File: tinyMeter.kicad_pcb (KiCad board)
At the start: 2 copper layers, 74.6 x 70 mm, 93 parts, among them J1 USB_MASTER, J2 DC_POWER, J3 USB_POWER, J4 USBA_OUT_2, J5 USBA_OUT_1, J6 DC_POWER, J7 Debug, J8 External antenna, Q1 100N03A, Q2 100N03A, Q3 100N03A, Q4 SS8050, SW1 SW_Push, SW2 SW_Push, SW3 SW_Push, SW4 SW_Push, SW5 SW_Push, SW6 Boot, SW7 Reset, U1 ESP32-S3, U2 INA219AxD, U3 INA219AxD, U4 INA219AxD, U5 AMS1117-3.3, Y1 Crystal_GND24

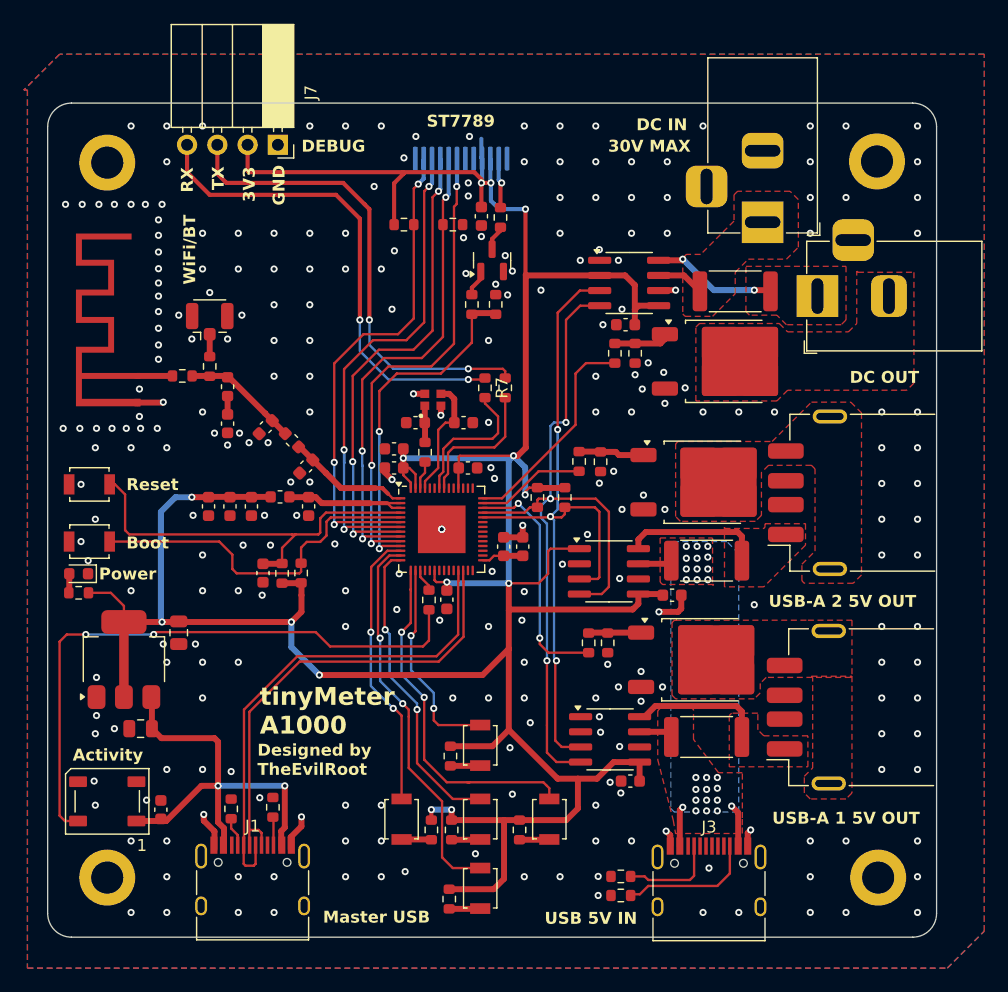
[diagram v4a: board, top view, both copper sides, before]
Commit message: Fix display connector orientation
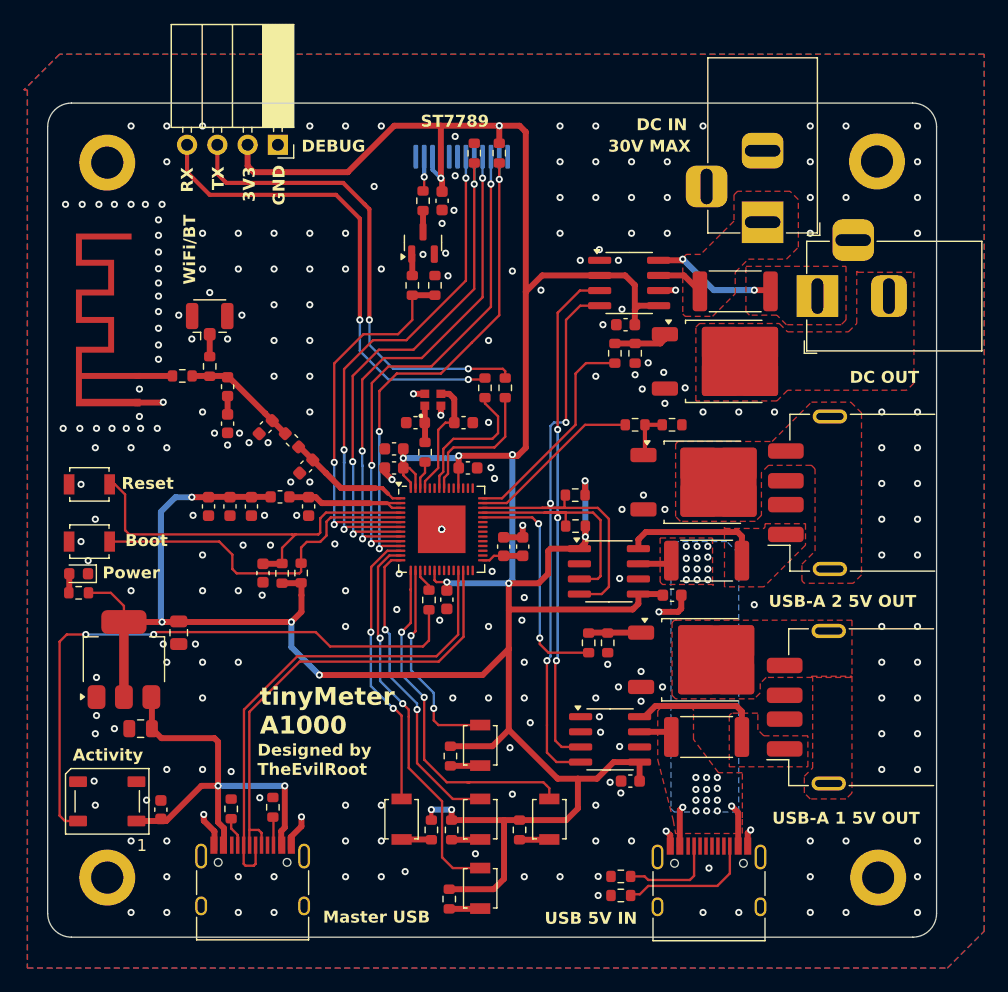
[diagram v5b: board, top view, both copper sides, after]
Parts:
- moved R34 10.0 mm to (176.9, 78.6), turned to -90 degrees
- moved DS1 8.84 mm to (173.8, 83.4), turned to 0 degrees
- moved R22 6.75 mm to (191.4, 101.4), turned to 0 degrees
- moved R30 6.65 mm to (170.5, 82.6)
- moved R33 6.26 mm to (174.8, 78.6), turned to 90 degrees
- moved Q4 5.98 mm to (170.5, 86.1)
- moved R21 5.62 mm to (188.3, 101.4), turned to 180 degrees
- moved R32 5.35 mm to (171.5, 89.7)
- moved R31 5.25 mm to (169.6, 89.7)
- moved R27 4.00 mm to (183.3, 109.9), turned to 0 degrees
- moved C6 3.55 mm to (172.1, 82.6)
- moved R26 0.90 mm to (183.3, 107.3), turned to 0 degrees
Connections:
- R26 pad 1: /METER_SDA -> /METER_SCL
- R27 pad 1: /METER_SCL -> /METER_SDA
- U1 pad 10: /DISPLAY_DC -> /DISPLAY_SDA
- U1 pad 11: /DISPLAY_BLK -> /DISPLAY_RST
- U1 pad 38: /METER_SDA -> /USBA_OUT_1_FETGATE
- U1 pad 39: /METER_SCL -> /METER_SDA
- U1 pad 40: /USBA_OUT_1_FETGATE -> /METER_SCL
- U1 pad 6: /DISPLAY_RST -> /DISPLAY_BLK
- U1 pad 7: /DISPLAY_SDA -> /DISPLAY_DC
- U1 pad 8: /DISPLAY_SCK -> /DISPLAY_CS
- U1 pad 9: /DISPLAY_CS -> /DISPLAY_SCK
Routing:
- net /USBA_OUT_2_FETGATE: track 9.19 -> 14.7 mm
- net /DISPLAY_CS: track 40.1 -> 43.4 mm
- net /DISPLAY_DC: track 39.9 -> 43.1 mm
- net /DISPLAY_BLK: track 29.1 -> 31.3 mm
- net /METER_SDA: track 61.0 -> 62.7 mm
- net /USBA_OUT2_GATE: track 5.52 -> 4.04 mm
- net /DISPLAY_LEDK: track 4.26 -> 2.92 mm
- net /DISPLAY_RST: track 41.2 -> 42.6 mm
- net /METER_SCL: track 65.5 -> 66.8 mm
- net /DISPLAY_SCK: track 40.3 -> 41.4 mm
- net /USBA_OUT_1_FETGATE: track 20.1 -> 19.3 mm
- net +3V3: track 278.8 -> 279.4 mm, vias 14 -> 15
- net GND: vias 240 -> 226

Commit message: Remove most of knockouts from silkscreen
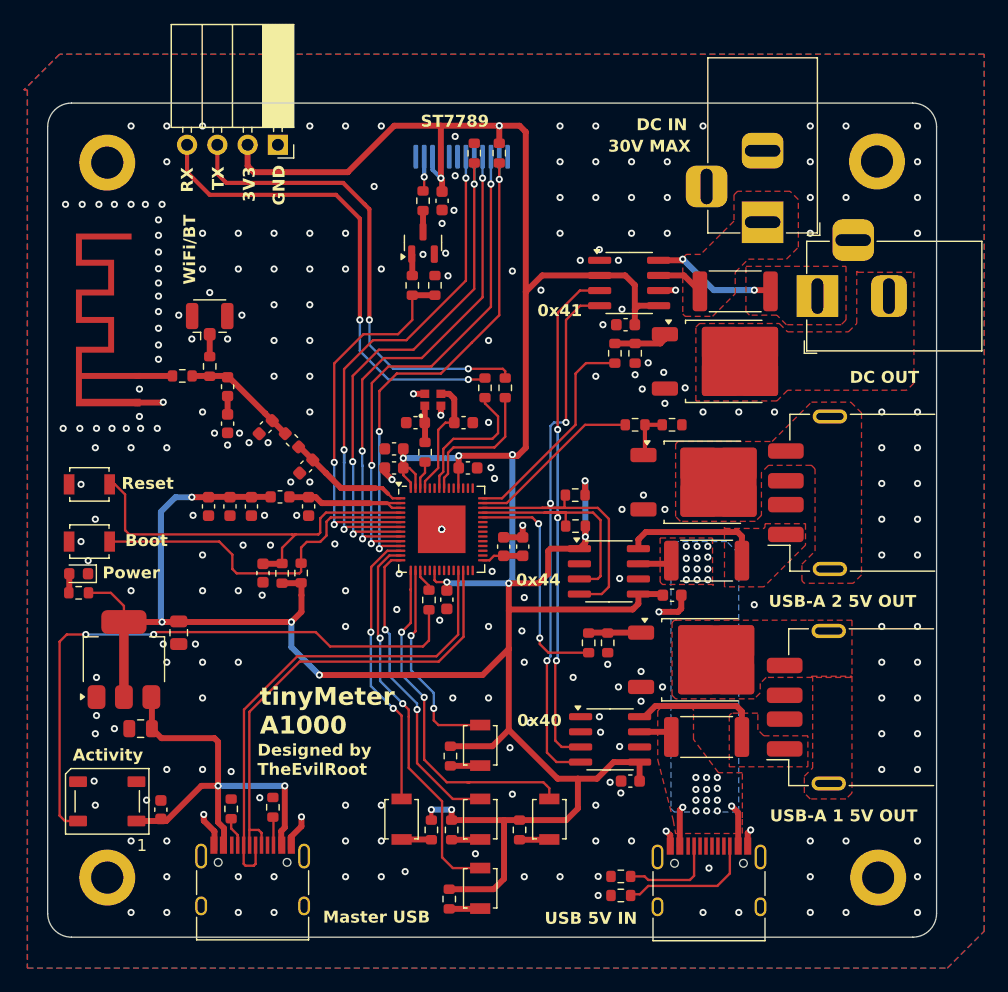
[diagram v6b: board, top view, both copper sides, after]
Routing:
- net GND: vias 226 -> 225
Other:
- board text added: "0x40"
- board text added: "0x41"
- board text added: "0x44"
- board text removed: "DEBUG"
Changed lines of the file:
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@@
 			(layer "F.SilkS"
 				(type "Top Silk Screen")
-				(color "White")
+				(color "Black")
 			)
 			(layer "F.Paste"
@@
 			(layer "F.Mask"
 				(type "Top Solder Mask")
-				(color "Black")
+				(color "White")
 				(thickness 0.01)
 			)
@@
 			(layer "B.Mask"
 				(type "Bottom Solder Mask")
-				(color "Black")
+				(color "White")
 				(thickness 0.01)
 			)
@@
 			(layer "B.SilkS"
 				(type "Bottom Silk Screen")
-				(color "White")
+				(color "Black")
 			)
 			(copper_finish "None")
@@
 		)
 	)
-	(gr_text "DEBUG"
-		(at 160.3 78.6 0)
-		(layer "F.SilkS" knockout)
-		(effects
-			(font
-				(size 1 1)
-				(thickness 0.2)
-				(bold yes)
-			)
-			(justify left bottom)
-		)
-	)
 	(gr_text "ST7789"
 		(at 170.3 76.5 0)
@@
 	)
 	(gr_text "USB-A 1 5V OUT"
-		(at 199.8 135 0)
-		(layer "F.SilkS" knockout)
+		(at 199.6 134.8 0)
+		(layer "F.SilkS")
 		(effects
 			(font
@@
 	(gr_text "Master USB"
 		(at 162.1 143.3 0)
-		(layer "F.SilkS" knockout)
+		(layer "F.SilkS")
 		(effects
 			(font
@@
 	(gr_text "3V3"
 		(at 156.5 82.7 90)
-		(layer "F.SilkS" knockout)
+		(layer "F.SilkS")
 		(effects
 			(font
@@
 	(gr_text "DC OUT"
 		(at 206.3 98 0)
-		(layer "F.SilkS" knockout)
+		(layer "F.SilkS")
 		(effects
 			(font
@@
 		)
 	)
+	(gr_text "0x41"
+		(at 180.1 92.4 0)
+		(layer "F.SilkS")
+		(effects
+			(font
+				(size 1 1)
+				(thickness 0.25)
+				(bold yes)
+			)
+			(justify left bottom)
+		)
+	)
 	(gr_text "GND"
 		(at 159 83 90)
-		(layer "F.SilkS" knockout)
+		(layer "F.SilkS")
 		(effects
 			(font
@@
 	(gr_text "Activity"
 		(at 141.1 129.7 0)
-		(layer "F.SilkS" knockout)
+		(layer "F.SilkS")
 		(effects
 			(font
@@
 	(gr_text "Reset"
 		(at 145.2 106.9 0)
-		(layer "F.SilkS" knockout)
+		(layer "F.SilkS")
 		(effects
 			(font
@@
 	(gr_text "DC IN"
 		(at 188.4 76.8 0)
-		(layer "F.SilkS" knockout)
+		(layer "F.SilkS")
 		(effects
 			(font
@@
 	(gr_text "Boot\n"
 		(at 145.5 111.7 0)
-		(layer "F.SilkS" knockout)
+		(layer "F.SilkS")
 		(effects
 			(font
@@
 	(gr_text "TX"
 		(at 153.9 81.7 90)
-		(layer "F.SilkS" knockout)
+		(layer "F.SilkS")
 		(effects
 			(font
@@
 		)
 	)
+	(gr_text "0x40"
+		(at 178.4 126.8 0)
+		(layer "F.SilkS")
+		(effects
+			(font
+				(size 1 1)
+				(thickness 0.25)
+				(bold yes)
+			)
+			(justify left bottom)
+		)
+	)
 	(gr_text "Power"
 		(at 143.6 114.4 0)
-		(layer "F.SilkS" knockout)
+		(layer "F.SilkS")
 		(effects
 			(font
@@
 	(gr_text "USB-A 2 5V OUT"
 		(at 199.5 116.8 0)
-		(layer "F.SilkS" knockout)
+		(layer "F.SilkS")
 		(effects
 			(font
@@
 		)
 	)
+	(gr_text "0x44"
+		(at 178.3 115 0)
+		(layer "F.SilkS")
+		(effects
+			(font
+				(size 1 1)
+				(thickness 0.25)
+				(bold yes)
+			)
+			(justify left bottom)
+		)
+	)
 	(gr_text "RX"
 		(at 151.3 81.9 90)
-		(layer "F.SilkS" knockout)
+		(layer "F.SilkS")
 		(effects
 			(font
@@
 	(gr_text "USB 5V IN"
 		(at 180.7 143.4 0)
-		(layer "F.SilkS" knockout)
+		(layer "F.SilkS")
 		(effects
 			(font
@@
 	)
 	(via
-		(at 179 124.325)
-		(size 0.6)
-		(drill 0.3)
-		(layers "F.Cu" "B.Cu")
-		(free yes)
-		(net 1)
-	)
-	(via
 		(at 161 76.325)
 		(size 0.6)
@@
 	)
 	(via
-		(at 185 124.325)
+		(at 183.1 122.6)
 		(size 0.6)
 		(drill 0.3)
@@
 	)
 	(via
-		(at 178.8 117.8)
+		(at 178.8 118.7)
 		(size 0.6)
 		(drill 0.3)

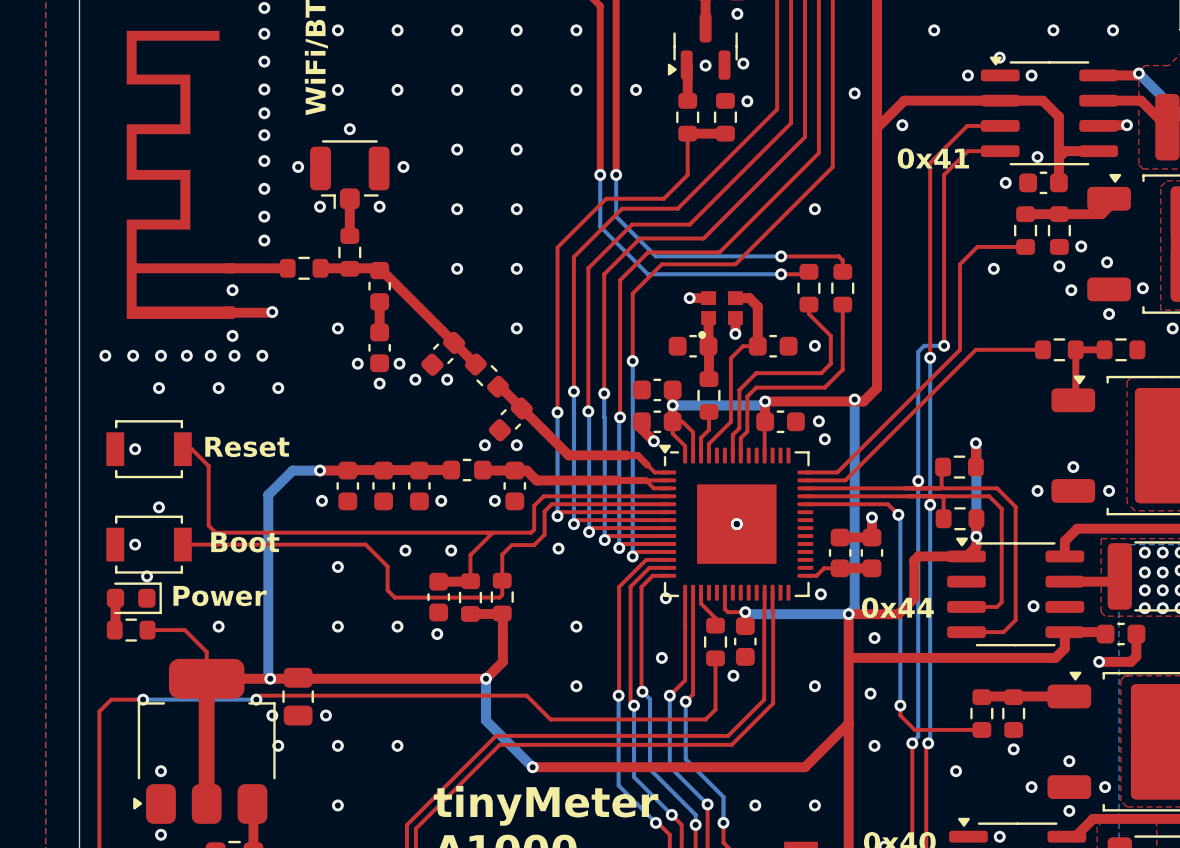
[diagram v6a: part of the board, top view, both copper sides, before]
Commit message: Tiny rerouting
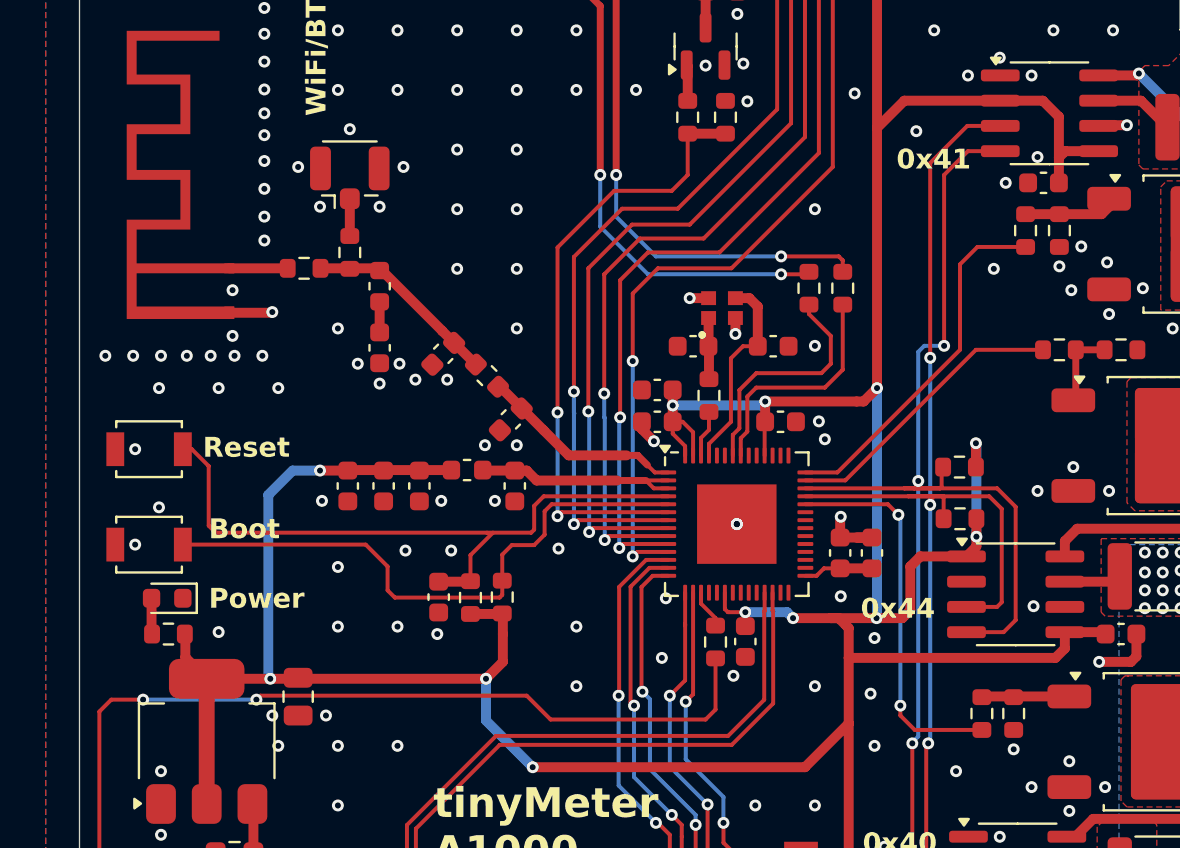
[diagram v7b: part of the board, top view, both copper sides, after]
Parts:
- moved R13 1.89 mm to (143.5, 115.7)
- moved D2 1.81 mm to (143.4, 113.9)
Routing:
- net GND: track 21.8 -> 22.7 mm, vias 225 -> 224
- net +3V3: track 279.4 -> 278.9 mm, vias 15 -> 16
